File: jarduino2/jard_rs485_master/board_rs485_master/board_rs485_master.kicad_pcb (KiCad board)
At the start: 2 copper layers, 99 x 69 mm, 2 parts

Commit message: Première visu placement future carte
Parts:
- added U1: MEGA_PRO_EMBED_CH340G_/_ATMEGA2560, bpc:BPC_ATMEGA2560_PRO, F.Cu at (132.7, 103.9)
- added U2: RtcArduino, bpc:BPC_RtcArduino, B.Cu at (122.5, 126.7)
- added U3: Arduino_Mod_RS485, bpc:BPC_Mod485, B.Cu at (166.4, 102.9)
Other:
- net class Default removed

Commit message: Création maître des oyas
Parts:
- removed REF** (x2): BPC_Trou4mm_Fixation, bpc:BPC_Trou4mm_Fixation
- removed U3: Arduino_Mod_RS485, bpc:BPC_Mod485
- added F1: Fuse, Fuse:Fuseholder_TR5_Littelfuse_No560_No460, F.Cu at (178.6, 77.0)
- added F2: Fuse, Fuse:Fuseholder_TR5_Littelfuse_No560_No460, F.Cu at (178.6, 88.0)
- added J1: POWER_12V, TerminalBlock_Phoenix:TerminalBlock_Phoenix_MKDS-1,5-2-5.08_1x02_P5.08mm_Horizontal, F.Cu at (152.6, 100.8)
- added J2: ON_OFF, TerminalBlock_Phoenix:TerminalBlock_Phoenix_MKDS-1,5-2-5.08_1x02_P5.08mm_Horizontal, F.Cu at (152.6, 112.7)
- added J3: POWER_OYAS_12V, TerminalBlock_Phoenix:TerminalBlock_Phoenix_MKDS-1,5-2-5.08_1x02_P5.08mm_Horizontal, F.Cu at (152.6, 124.5)
- added J4: BUS_OYAS, TerminalBlock_Phoenix:TerminalBlock_Phoenix_MKDS-1,5-4-5.08_1x04_P5.08mm_Horizontal, F.Cu at (164.8, 118.5)
- added J5: Leds RGB, Connector_JST:JST_XH_B3B-XH-AM_1x03_P2.50mm_Vertical, F.Cu at (164.7, 127.5)
- added Q1: BPC_2N2222A, Package_TO_SOT_THT:TO-92, F.Cu at (123.8, 122.8)
- added Q2: BPC_IPP034N03L, Package_TO_SOT_THT:TO-220-3_Vertical, F.Cu at (176.4, 128.0)
- added Q3: BC327, Package_TO_SOT_THT:TO-92_Inline, F.Cu at (123.8, 128.6)
- added R1: 10k, Resistor_THT:R_Axial_DIN0204_L3.6mm_D1.6mm_P7.62mm_Horizontal, F.Cu at (139.9, 96.2)
- added R10: R, Resistor_THT:R_Axial_DIN0204_L3.6mm_D1.6mm_P7.62mm_Horizontal, F.Cu at (139.9, 124.5)
- added R11: R, Resistor_THT:R_Axial_DIN0204_L3.6mm_D1.6mm_P7.62mm_Horizontal, F.Cu at (139.9, 127.7)
- added R12: R, Resistor_THT:R_Axial_DIN0204_L3.6mm_D1.6mm_P7.62mm_Horizontal, F.Cu at (139.9, 130.8)
- added R13: R, Resistor_THT:R_Axial_DIN0204_L3.6mm_D1.6mm_P7.62mm_Horizontal, F.Cu at (139.9, 134.0)
- added R2: 10k, Resistor_THT:R_Axial_DIN0204_L3.6mm_D1.6mm_P7.62mm_Horizontal, F.Cu at (139.9, 99.3)
- added R3: R, Resistor_THT:R_Axial_DIN0204_L3.6mm_D1.6mm_P7.62mm_Horizontal, F.Cu at (139.9, 102.5)
- added R4: R, Resistor_THT:R_Axial_DIN0204_L3.6mm_D1.6mm_P7.62mm_Horizontal, F.Cu at (139.9, 105.6)
- added R5: R, Resistor_THT:R_Axial_DIN0204_L3.6mm_D1.6mm_P7.62mm_Horizontal, F.Cu at (139.9, 108.8)
- added R6: R, Resistor_THT:R_Axial_DIN0204_L3.6mm_D1.6mm_P7.62mm_Horizontal, F.Cu at (139.9, 111.9)
- added R7: R, Resistor_THT:R_Axial_DIN0204_L3.6mm_D1.6mm_P7.62mm_Horizontal, F.Cu at (139.9, 115.1)
- added R8: R, Resistor_THT:R_Axial_DIN0204_L3.6mm_D1.6mm_P7.62mm_Horizontal, F.Cu at (139.9, 118.2)
- added R9: R, Resistor_THT:R_Axial_DIN0204_L3.6mm_D1.6mm_P7.62mm_Horizontal, F.Cu at (139.9, 121.4)
- added U4: BPC_Mod485, bpc:BPC_Mod485, F.Cu at (125.9, 74.6)
- U1: value MEGA_PRO_EMBED_CH340G_/_ATMEGA2560 -> RtcArduino; footprint bpc:BPC_ATMEGA2560_PRO -> bpc:BPC_RtcArduino
- U2: value RtcArduino -> BPC_Alim3_3V; footprint bpc:BPC_RtcArduino -> bpc:BPC_Alim3_3V; moved to F.Cu
- moved U2 50.6 mm to (163.1, 96.4)
- moved U1 28.8 mm to (140.0, 76.0), turned to 0 degrees
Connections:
- U2 pad 1: unconnected-(U2-GND-Pad1) -> Net-(F1-Pad1)
- U2 pad 2: unconnected-(U2-VCC-Pad2) -> Net-(F1-Pad1)
- U2 pad 3: unconnected-(U2-SDA-Pad3) -> GND
- U2 pad 4: unconnected-(U2-SCL-Pad4) -> GND
- U2 pad 5: unconnected-(U2-SQW-Pad5) -> GND
- U2 pad 6: unconnected-(U2-32K-Pad6) -> GND
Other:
- board outline removed

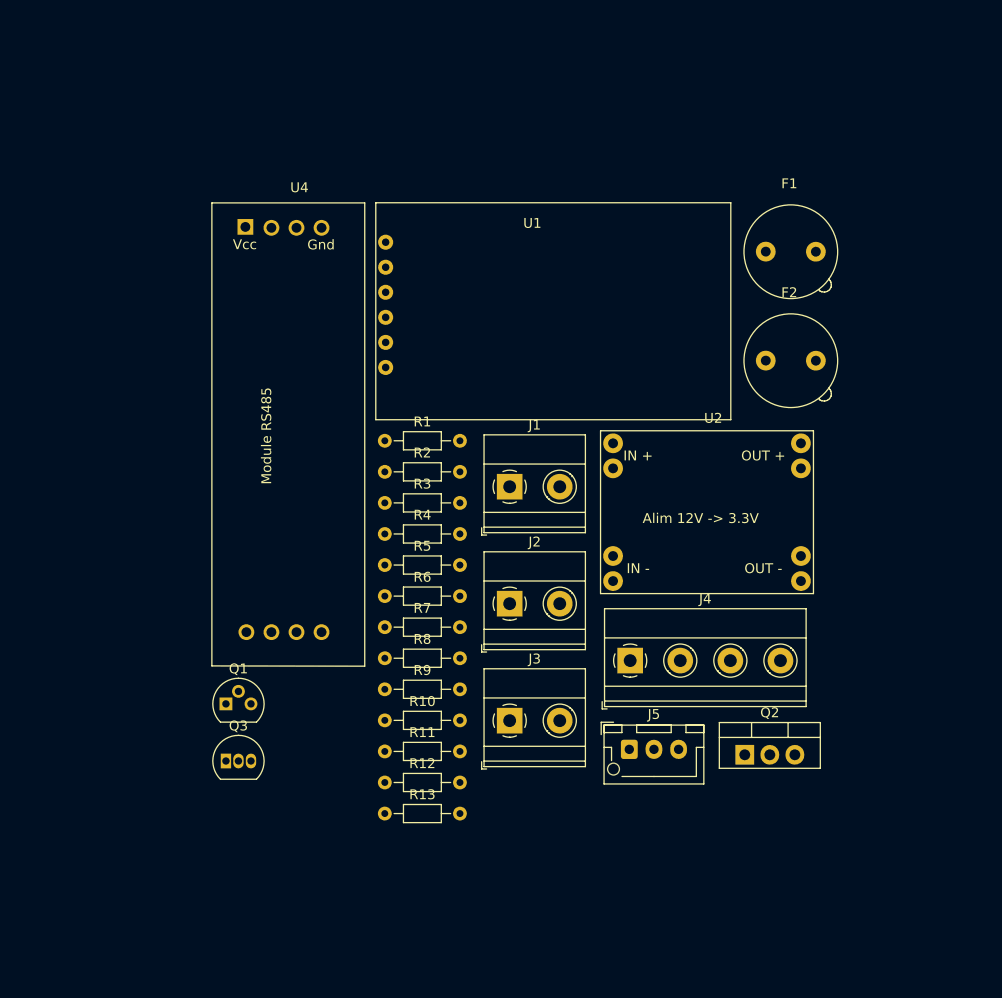
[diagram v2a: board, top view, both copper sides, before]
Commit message: Routage carte + Ajout ESP 01 + ...
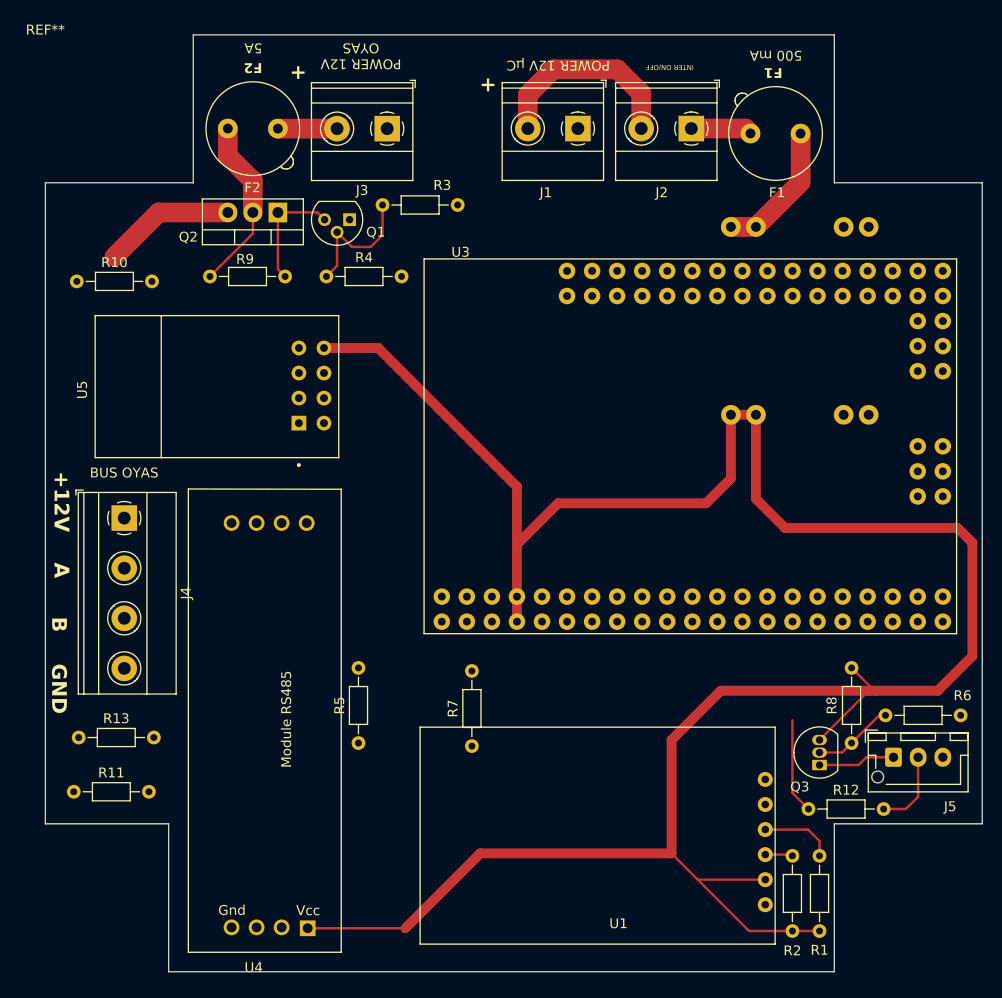
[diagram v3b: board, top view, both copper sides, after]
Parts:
- added REF**: BPC_BoiteDeriv_110x110x60, bpc:BPC_BoiteDeriv_110x110x60, F.Cu at (105.5, 55.0)
- added U3: BPC_ATMEGA2560_PRO, bpc:BPC_ATMEGA2560_PRO_MINI, F.Cu at (170.9, 96.7)
- added U5: BPC_ESP8266-01_ESP-01, bpc:BPC_XCVR_ESP8266-01_ESP-01, F.Cu at (122.9, 90.6)
- U2: moved to B.Cu
- moved U1 77.4 mm to (178.5, 143.2), turned to 180 degrees
- moved Q2 72.6 mm to (129.1, 73.0), turned to 180 degrees
- moved U4 71.2 mm to (132.0, 145.5), turned to 180 degrees
- moved R1 66.4 mm to (184.0, 145.9), turned to 90 degrees
- moved R2 62.3 mm to (181.2, 145.9), turned to 90 degrees
- moved J3 61.3 mm to (140.2, 64.5), turned to 180 degrees
- moved Q3 60.2 mm to (184.0, 129.0), turned to 90 degrees
- moved R6 59.6 mm to (198.3, 124.0), turned to 180 degrees
- moved F2 59.4 mm to (124.0, 64.5)
- moved R10 54.4 mm to (108.7, 80.0)
- moved J4 53.3 mm to (113.5, 104.0), turned to -90 degrees
- moved J2 51.6 mm to (171.0, 64.5), turned to 180 degrees
- moved Q1 50.7 mm to (136.3, 73.7), turned to 180 degrees
- moved R8 47.3 mm to (187.2, 119.2), turned to -90 degrees
- moved R9 45.5 mm to (122.2, 79.5)
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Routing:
- net +3.3V: track 0.00 -> 242.5 mm
- net Net-(J1-Pin_2): track 0.00 -> 20.6 mm
- net Net-(Q2-D): track 0.00 -> 17.9 mm
- net Net-(F1-Pad1): track 0.00 -> 13.9 mm
- net Net-(Q1-Pad2): track 0.00 -> 13.7 mm
- net Net-(J4-Pin_1): track 0.00 -> 13.4 mm
- net Net-(Q2-G): track 0.00 -> 11.8 mm
- net DATA_LEDS: track 0.00 -> 9.68 mm
- net Net-(Q3-B): track 0.00 -> 8.25 mm
- net Net-(J5-Pin_2): track 0.00 -> 8.02 mm
- net Net-(J5-Pin_1): track 0.00 -> 7.88 mm
- net SCL: track 0.00 -> 7.48 mm
- net Net-(J2-Pin_1): track 0.00 -> 6.21 mm
- net Net-(J3-Pin_2): track 0.00 -> 6.00 mm
- net SDA: track 0.00 -> 2.80 mm
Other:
- board outline added: 95 x 95 mm
- board text added: "+"
- board text added: "+12V"
- board text added: "500 mA"
- board text added: "5A"
- board text added: "A"
- board text added: "B"
- board text added: "BUS OYAS"
- board text added: "F1"
- board text added: "F2"
- board text added: "GND"
- board text added: "INTER ON/OFF"
- board text added: "POWER 12V OYAS"
- board text added: "POWER 12V µC"

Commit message: Le maître des oyas devient un shield ATMEGA
- RTC
- ESP
- LEDs RGB
- Alim 5V
- RS485
- Alim 12V commutée
- Mais manque SD card....
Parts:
- removed REF**: BPC_BoiteDeriv_110x110x60, bpc:BPC_BoiteDeriv_110x110x60
- removed U5: BPC_ESP8266-01_ESP-01, bpc:BPC_XCVR_ESP8266-01_ESP-01
- added C1: 10µF, Capacitor_THT:CP_Radial_D4.0mm_P2.00mm, F.Cu at (26.7, 89.3)
- added C2: 100nF, Capacitor_THT:C_Disc_D5.0mm_W2.5mm_P2.50mm, F.Cu at (26.9, 84.5)
- added C4: 100µF, Capacitor_THT:C_Disc_D5.0mm_W2.5mm_P2.50mm, F.Cu at (44.8, 63.2)
- added C5: 100nF, Capacitor_THT:C_Disc_D5.0mm_W2.5mm_P2.50mm, F.Cu at (45.5, 69.0)
- added C6: 100nF, Capacitor_THT:C_Disc_D5.0mm_W2.5mm_P2.50mm, F.Cu at (16.5, 58.5)
- added C7: 100nF, Capacitor_THT:C_Disc_D5.0mm_W2.5mm_P2.50mm, F.Cu at (-10.9, 61.1)
- added C8: 10µF, Capacitor_THT:CP_Radial_D4.0mm_P2.00mm, F.Cu at (74.7, 89.0)
- added D1: D, Diode_THT:D_A-405_P2.54mm_Vertical_AnodeUp, F.Cu at (64.2, 78.0)
- added D2: D, Diode_THT:D_A-405_P2.54mm_Vertical_AnodeUp, F.Cu at (137.8, 105.5)
- added D3: D, Diode_THT:D_A-405_P2.54mm_Vertical_AnodeUp, F.Cu at (133.3, 83.0)
- added Q4: BC327, Package_TO_SOT_THT:TO-92_Inline, F.Cu at (83.0, 89.2)
- added R14: 220, Resistor_THT:R_Axial_DIN0204_L3.6mm_D1.6mm_P7.62mm_Horizontal, F.Cu at (90.8, 95.1)
- added R15: 100k, Resistor_THT:R_Axial_DIN0204_L3.6mm_D1.6mm_P7.62mm_Horizontal, F.Cu at (88.2, 87.4)
- added XA1: Arduino_Mega2560_Shield, bpc:BPC_Arduino_Mega2560_Shield, F.Cu at (58.5, 117.5)
- R12, R3: value R -> 100
- R13: value R -> 128
- R4, R8, R9: value R -> 100k
- R5, R6, R7: value R -> 220
- U2: value BPC_Alim3_3V -> BPC_Alim5V; footprint bpc:BPC_Alim3_3V -> bpc:BPC_Alim5V; moved to F.Cu
- U3: value BPC_ATMEGA2560_PRO -> BPC_ESP8266-01_ESP-01; footprint bpc:BPC_ATMEGA2560_PRO_MINI -> bpc:BPC_XCVR_ESP8266-01_ESP-01
- moved Q3 159.5 mm to (45.8, 49.5)
- moved R12 159.5 mm to (44.6, 54.0)
- moved R6 159.5 mm to (60.1, 44.5)
- moved R8 159.5 mm to (49.0, 39.7)
- moved J5 142.0 mm to (63.0, 67.8), turned to -90 degrees
- moved R1 125.6 mm to (102.0, 50.8)
- moved R2 125.6 mm to (99.2, 50.8)
- moved F1 119.5 mm to (64.3, 85.0), turned to -90 degrees
- moved J2 111.6 mm to (64.0, 96.2), turned to -90 degrees
- moved U1 109.4 mm to (94.0, 73.8), turned to 0 degrees
- moved J1 104.7 mm to (64.2, 107.9), turned to -90 degrees
- moved U2 103.6 mm to (71.5, 71.0), turned to 0 degrees
- moved U3 92.0 mm to (79.2, 104.2), turned to 180 degrees
- moved R11 50.7 mm to (138.2, 90.8), turned to 90 degrees
- moved U4 44.5 mm to (132.7, 101.0), turned to -90 degrees
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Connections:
- F1 pad 1: Net-(F1-Pad1) -> Net-(D1-A)
- F2 pad 1: Net-(Q2-D) -> Net-(D3-A)
- J4 pad 2: Net-(J4-Pin_2) -> A
- J4 pad 3: Net-(J4-Pin_3) -> B
- Q2 pad 2: Net-(Q2-D) -> Net-(D3-K)
- Q3 pad 3: +3.3V -> +5V
- R1 pad 1: +3.3V -> +5V
- R10 pad 2: Net-(J4-Pin_2) -> A
- R11 pad 1: Net-(J4-Pin_3) -> B
- R13 pad 1: Net-(J4-Pin_2) -> A
- R13 pad 2: Net-(J4-Pin_3) -> B
- R2 pad 1: +3.3V -> +5V
- R5 pad 1: +3.3V -> +5V
- R5 pad 2: Net-(J4-Pin_3) -> A
- R7 pad 1: Net-(J4-Pin_3) -> B
- R8 pad 1: +3.3V -> +5V
- R9 pad 1: Net-(Q2-D) -> Net-(D3-K)
- U1 pad 2: +3.3V -> +5V
- U2 pad 1: Net-(F1-Pad1) -> Net-(D1-K)
- U2 pad 2: Net-(F1-Pad1) -> Net-(D1-K)
- U2 pad 7: +3.3V -> +5V
- U2 pad 8: +3.3V -> +5V
- U4 pad 1: +3.3V -> +5V
- U4 pad 2: Net-(J4-Pin_3) -> B
- U4 pad 3: Net-(J4-Pin_2) -> A
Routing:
- net +3.3V: track 242.5 -> 0.00 mm
- net Net-(J1-Pin_2): track 20.6 -> 0.00 mm
- net Net-(Q2-D): track 17.9 -> 0.00 mm
- net Net-(F1-Pad1): track 13.9 -> 0.00 mm
- net Net-(C6-Pad1): track 13.7 -> 0.00 mm
- net Net-(D2-K): track 13.4 -> 0.00 mm
- net Net-(Q2-G): track 11.8 -> 0.00 mm
- net DATA_LEDS: track 9.68 -> 0.00 mm
- net Net-(Q3-B): track 8.25 -> 0.00 mm
- net Net-(J5-Pin_2): track 8.02 -> 0.00 mm
- net Net-(J5-Pin_1): track 7.88 -> 0.00 mm
- net SCL: track 7.48 -> 0.00 mm
- net Net-(J2-Pin_1): track 6.21 -> 0.00 mm
- net Net-(J3-Pin_2): track 6.00 -> 0.00 mm
- net SDA: track 2.80 -> 0.00 mm
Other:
- board size 95 x 95 mm -> 101.5 x 53.2 mm
- board text removed: "A"

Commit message: Candidate pour revue du master Oyas (avec modules en tant que shield MEGA)
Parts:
- removed R11: R, Resistor_THT:R_Axial_DIN0204_L3.6mm_D1.6mm_P7.62mm_Horizontal
- added C10: 1nF, Capacitor_THT:C_Disc_D5.0mm_W2.5mm_P2.50mm, F.Cu at (127.0, 61.4)
- added C11: 100nF, Capacitor_THT:C_Disc_D5.0mm_W2.5mm_P2.50mm, F.Cu at (135.3, 112.6)
- added C12: 100nF, Capacitor_THT:C_Disc_D5.0mm_W2.5mm_P2.50mm, F.Cu at (88.6, 81.5)
- added C13: 10µF, Capacitor_THT:CP_Radial_D4.0mm_P2.00mm, F.Cu at (82.2, 73.5)
- added C14: 100nF, Capacitor_THT:C_Disc_D5.0mm_W2.5mm_P2.50mm, F.Cu at (136.1, 72.5)
- added C15: 10µF, Capacitor_THT:CP_Radial_D4.0mm_P2.00mm, F.Cu at (140.9, 80.2)
- added C3: 1nF, Capacitor_THT:C_Disc_D5.0mm_W2.5mm_P2.50mm, F.Cu at (127.0, 54.6)
- added C9: 1nF, Capacitor_THT:C_Disc_D5.0mm_W2.5mm_P2.50mm, F.Cu at (127.0, 58.1)
- added D4: SM712_SOT23, Package_TO_SOT_SMD:SOT-23, B.Cu at (189.7, 73.8)
- added D5: SD12_SOD323, Diode_SMD:D_SOD-323, B.Cu at (197.2, 73.7)
- added D6: SD12_SOD323, Diode_SMD:D_SOD-323, B.Cu at (170.4, 54.0)
- added J6: Button, Connector_PinHeader_2.54mm:PinHeader_1x02_P2.54mm_Vertical, F.Cu at (130.5, 75.1)
- added R16: 100, Resistor_THT:R_Axial_DIN0204_L3.6mm_D1.6mm_P7.62mm_Horizontal, B.Cu at (134.9, 53.1)
- added R17: 100, Resistor_THT:R_Axial_DIN0204_L3.6mm_D1.6mm_P7.62mm_Horizontal, B.Cu at (135.1, 58.0)
- added R18: 100, Resistor_THT:R_Axial_DIN0204_L3.6mm_D1.6mm_P7.62mm_Horizontal, B.Cu at (135.1, 60.7)
- added U5: LM1117DT-3.3, Package_TO_SOT_THT:TO-220-3_Vertical, F.Cu at (86.6, 78.4)
- C4: footprint Capacitor_THT:C_Disc_D5.0mm_W2.5mm_P2.50mm -> Capacitor_THT:CP_Radial_D8.0mm_P3.80mm
- D3: footprint Diode_THT:D_A-405_P2.54mm_Vertical_AnodeUp -> Diode_THT:D_A-405_P12.70mm_Horizontal
- J2: value ON_OFF -> Log; footprint TerminalBlock_Phoenix:TerminalBlock_Phoenix_MKDS-1,5-2-5.08_1x02_P5.08mm_Horizontal -> Connector_JST:JST_XH_B4B-XH-AM_1x04_P2.50mm_Vertical
- moved C7 189.5 mm to (178.3, 51.0), turned to -90 degrees
- moved C6 168.3 mm to (178.3, 105.1), turned to -90 degrees
- moved C8 114.5 mm to (182.8, 51.2), turned to -90 degrees
- moved R12 101.3 mm to (137.1, 95.3), turned to -90 degrees
- moved Q3 99.9 mm to (131.3, 101.2), turned to 180 degrees
- moved R8 95.1 mm to (124.2, 97.9), turned to 0 degrees
- moved C1 87.1 mm to (106.3, 53.7), turned to -90 degrees
- moved J5 82.7 mm to (135.2, 108.0), turned to 180 degrees
- moved R6 82.1 mm to (124.2, 95.7), turned to 0 degrees
- moved C2 81.5 mm to (102.3, 53.5), turned to -90 degrees
- moved J2 80.0 mm to (140.8, 73.8), turned to 0 degrees
- moved R4 73.3 mm to (174.5, 102.2)
- moved U1 68.8 mm to (162.6, 79.4), turned to -90 degrees
- moved Q1 68.3 mm to (182.9, 107.6), turned to 90 degrees
- moved R2 67.7 mm to (162.6, 74.5), turned to 180 degrees
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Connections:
- F1 pad 2: Net-(J2-Pin_1) -> Net-(J1-Pin_2)
- J2 pad 1: Net-(J2-Pin_1) -> +5V
- J2 pad 2: Net-(J1-Pin_2) -> TX_LOG
- Q4 pad 1: POWER_3.3 -> Net-(Q4-C)
- U4 pad 5: RS485_TX -> Net-(U4-DI)
- U4 pad 6: TX_EN -> Net-(U4-DE)
- U4 pad 7: TX_EN -> Net-(U4-DE)
- U4 pad 8: RS485_RX -> Net-(U4-RO)
- XA1 pad 5V1: unconnected-(XA1-5V-Pad5V1) -> +5V
- XA1 pad 5V3: unconnected-(XA1-5V-Pad5V3) -> +5V
- XA1 pad 5V4: unconnected-(XA1-5V-Pad5V4) -> +5V
- XA1 pad D14: unconnected-(XA1-D14_TX3-PadD14) -> TX_LOG
- XA1 pad D15: unconnected-(XA1-D15_RX3-PadD15) -> RX_LOG
- XA1 pad D16: unconnected-(XA1-D16_TX2-PadD16) -> TX_WIFI
- XA1 pad D17: unconnected-(XA1-D17_RX2-PadD17) -> RX_WIFI
- XA1 pad D18: unconnected-(XA1-D18_TX1-PadD18) -> RS485_TX
- XA1 pad D19: unconnected-(XA1-D19_RX1-PadD19) -> RS485_RX
- XA1 pad D2: unconnected-(XA1-D2_INT0-PadD2) -> TEST_BTN
- XA1 pad D20: unconnected-(XA1-D20_SDA-PadD20) -> SDA
- XA1 pad D21: unconnected-(XA1-D21_SCL-PadD21) -> SCL
- XA1 pad D4: unconnected-(XA1-PadD4) -> DATA_LEDS
- XA1 pad D5: unconnected-(XA1-PadD5) -> CMD_LEDS_PWR
- XA1 pad D6: unconnected-(XA1-PadD6) -> TX_EN
- XA1 pad D7: unconnected-(XA1-PadD7) -> CMD_WIFI_PWR
- XA1 pad D8: unconnected-(XA1-PadD8) -> CMD_OYAS_PWR
- XA1 pad GND1: unconnected-(XA1-GND-PadGND1) -> GND
- XA1 pad GND2: unconnected-(XA1-GND-PadGND2) -> GND
- XA1 pad GND3: unconnected-(XA1-GND-PadGND3) -> GND
- XA1 pad GND5: unconnected-(XA1-GND-PadGND5) -> GND
- XA1 pad GND6: unconnected-(XA1-GND-PadGND6) -> GND
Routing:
- net +5V: track 0.00 -> 262.0 mm
- net CMD_OYAS_PWR: track 0.00 -> 94.7 mm, vias 0 -> 1
- net RX_WIFI: track 0.00 -> 73.0 mm, vias 0 -> 2
- net POWER_3.3: track 0.00 -> 69.6 mm
- net A: track 0.00 -> 65.4 mm
- net TX_WIFI: track 0.00 -> 53.7 mm, vias 0 -> 2
- net B: track 0.00 -> 45.4 mm
- net RS485_RX: track 0.00 -> 41.6 mm
- net DATA_LEDS: track 0.00 -> 32.7 mm, vias 0 -> 1
- net CMD_LEDS_PWR: track 0.00 -> 27.2 mm, vias 0 -> 1
- net TX_EN: track 0.00 -> 26.3 mm
- net CMD_WIFI_PWR: track 0.00 -> 21.2 mm
- net Net-(D2-K): track 0.00 -> 20.2 mm
- net Net-(Q2-G): track 0.00 -> 18.2 mm
- net Net-(D3-K): track 0.00 -> 17.5 mm
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- added copper zone on B.Cu, net GND
- added copper zone on F.Cu, net GND
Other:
- board size 101.5 x 53.2 mm -> 132.4 x 70.8 mm
- board text added: "+5V"
- board text added: "A"
- board text added: "Bus OYAs"
- board text added: "Button"
- board text added: "LEDs"
- board text added: "Log"
- board text added: "Maître des OYAs Rev A0 BPC 2024"
- board text added: "POWER"
- board text added: "POWER OYAS"
- board text removed: "+"
- board text removed: "500 mA"
- board text removed: "5A"
- board text removed: "BUS OYAS"
- board text removed: "F1"
- board text removed: "F2"
- board text removed: "INTER ON/OFF"
- board text removed: "POWER 12V OYAS"
- board text removed: "POWER 12V µC"

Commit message: Finalisation dossier
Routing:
- net GND: vias 132 -> 136
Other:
- board text added: "(500 mA)"
- board text added: "(5A)"
- board text added: "31/03/2024"
- board text added: "ESP01 Wifi"
- board text added: "RTC"
- board text added: "RX"
- board text added: "TX"
- board text added: "[NM]"
